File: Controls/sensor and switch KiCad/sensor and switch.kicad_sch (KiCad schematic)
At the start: 27 parts, among them U10 Encoder Breakout Board, U12 Spark MAX Motor Controller, U13 Max Breakout Board, U14 Encoder Breakout Board, U16 Spark MAX Motor Controller, U17 Max Breakout Board, U18 Encoder Breakout Board, U2 Jetson Nano, U20 Spark MAX Motor Controller, U21 Max Breakout Board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

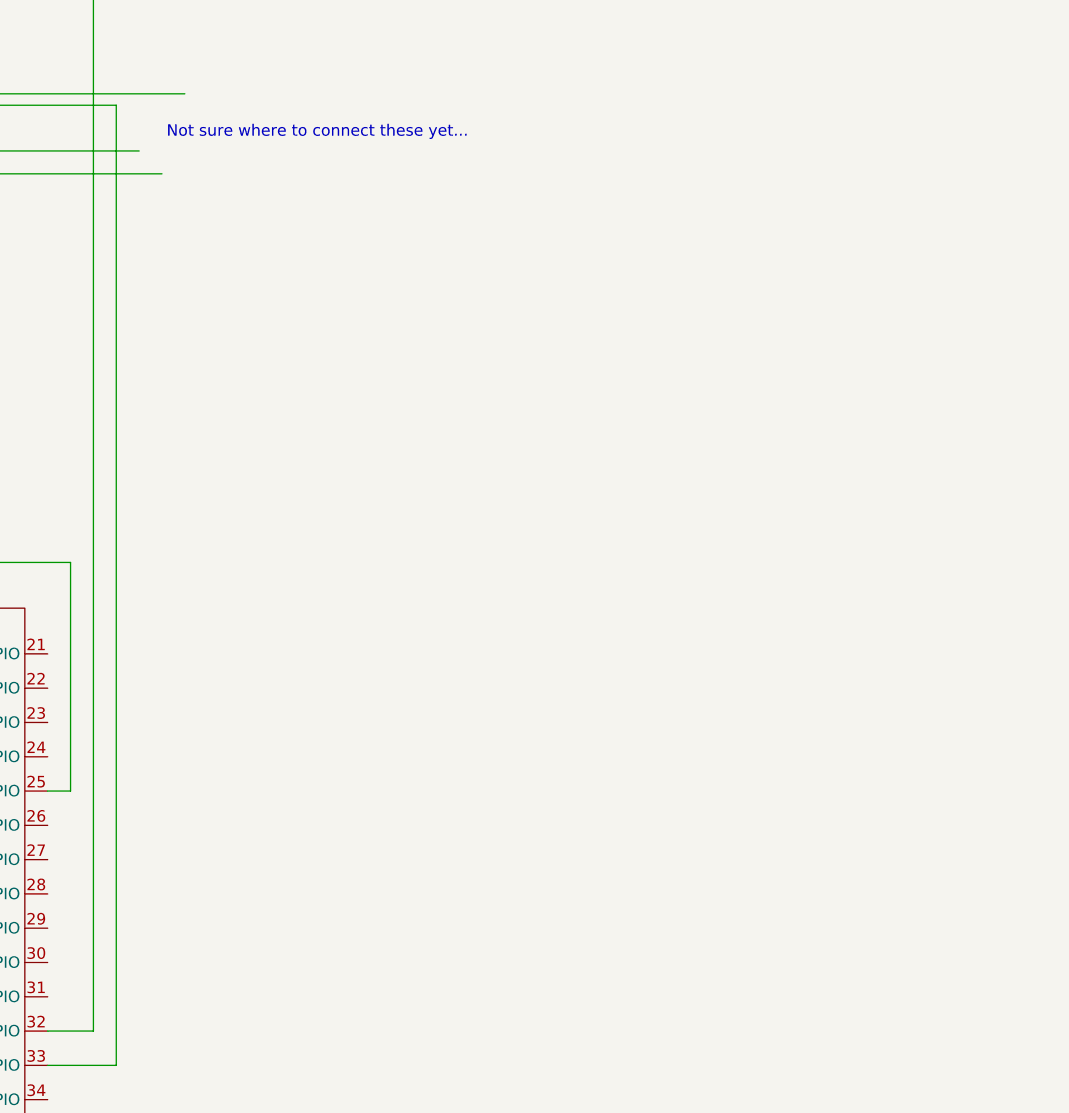
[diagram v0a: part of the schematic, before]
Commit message: Added linear actuator
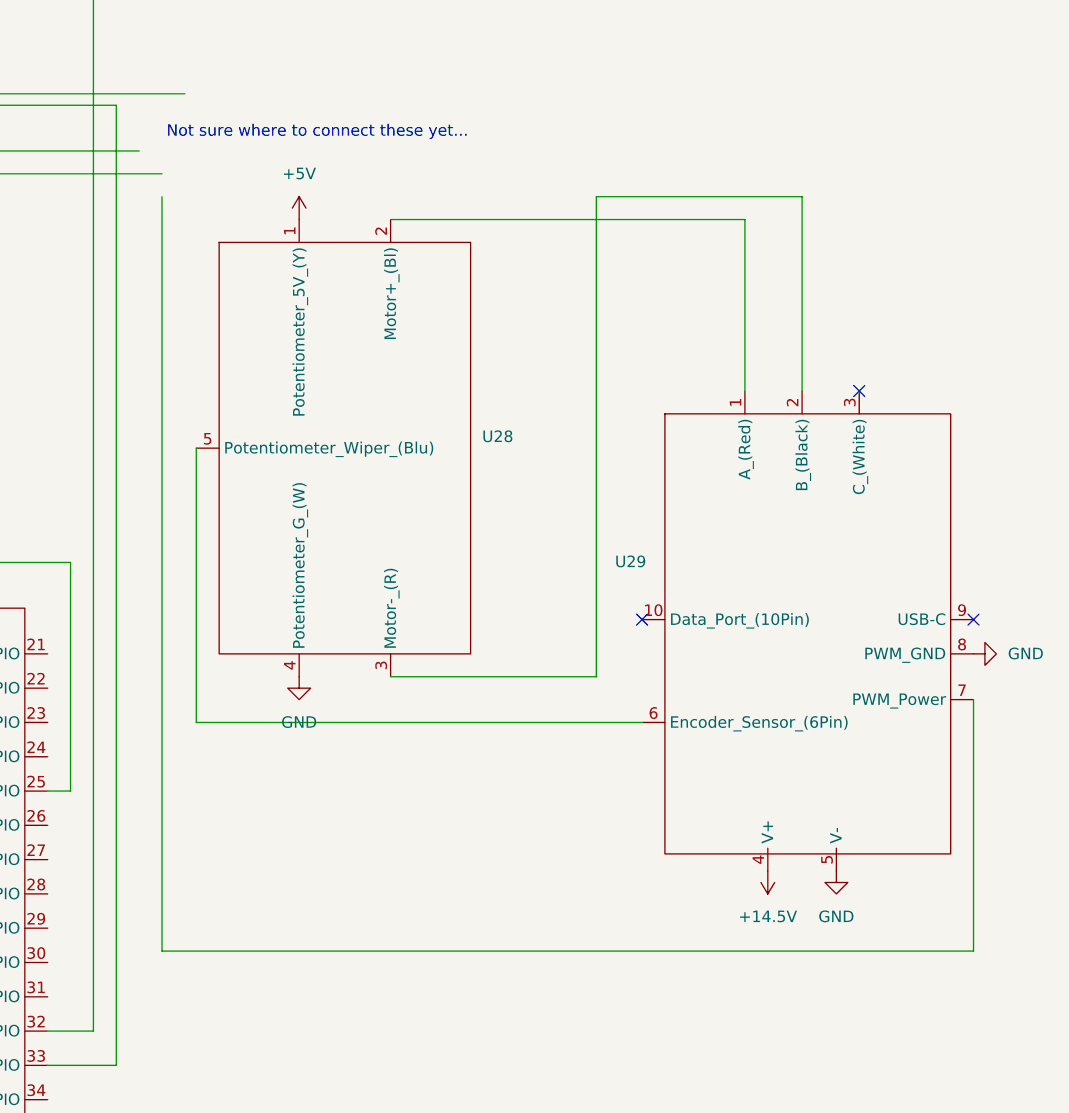
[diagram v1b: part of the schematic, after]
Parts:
- added U28: ~, symbol Lunabotics 2025-26:Feedback_Linear_Actuator
- added U29: ~, symbol Lunabotics 2025-26:Spark_MAX_Motor_Controller
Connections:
- net +5V: now also U28.1 (Potentiometer_5V_(Y))
- net GND: now also U28.4 (Potentiometer_G_(W)), U29.5 (V-), U29.8 (PWM_GND)
- new net: U28.2 (Motor+_(Bl)), U29.1 (A_(Red))
- new net: U28.3 (Motor-_(R)), U29.2 (B_(Black))
- new net: U28.5 (Potentiometer_Wiper_(Blu)), U29.6 (Encoder_Sensor_(6Pin))
- new net +14.5V: U29.4 (V+)
- no-connect marks 89 -> 92

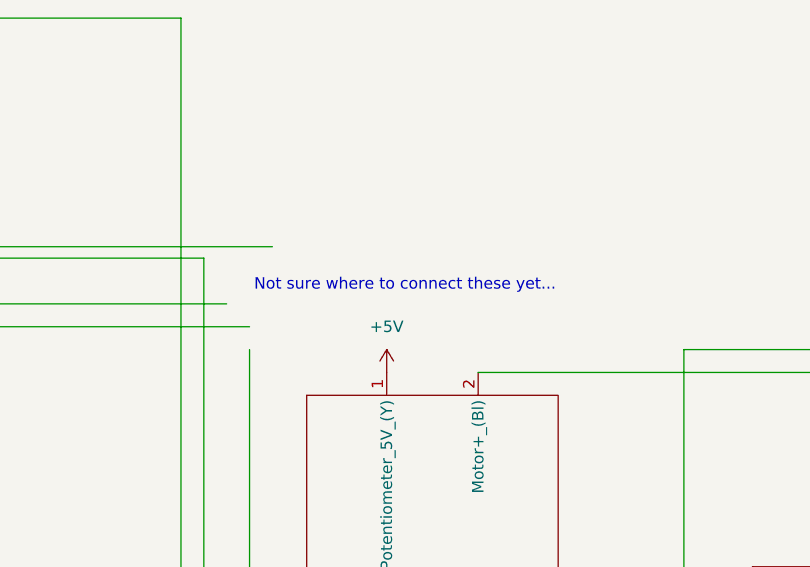
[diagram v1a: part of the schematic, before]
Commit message: Ported Linear Actuator to other schematics
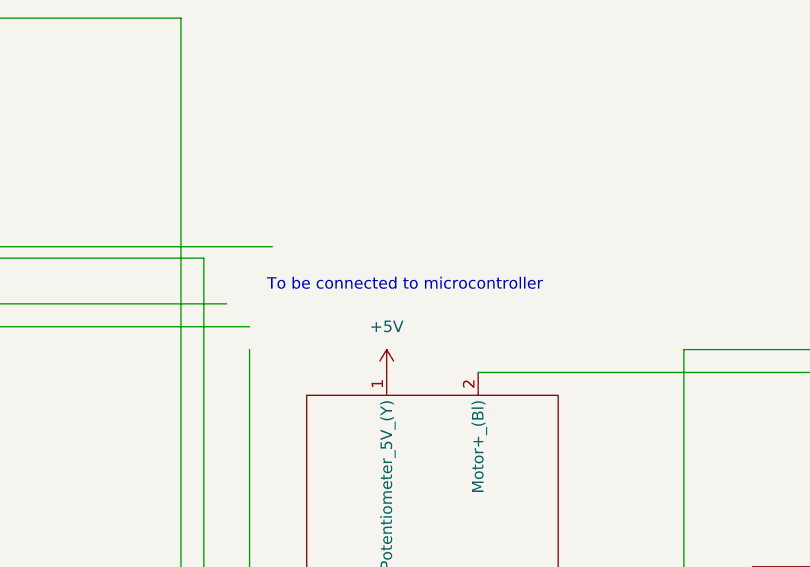
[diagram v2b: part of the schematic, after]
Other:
- note added: "To be connected to microcontroller"
- note removed: "Not sure where to connect these yet..."
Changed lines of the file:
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@@
 	(generator_version "9.0")
 	(paper "A2")
-	(text "Not sure where to connect these yet..."
+	(text "To be connected to microcontroller"
 		(exclude_from_sim no)
 		(at 488.442 165.608 0)

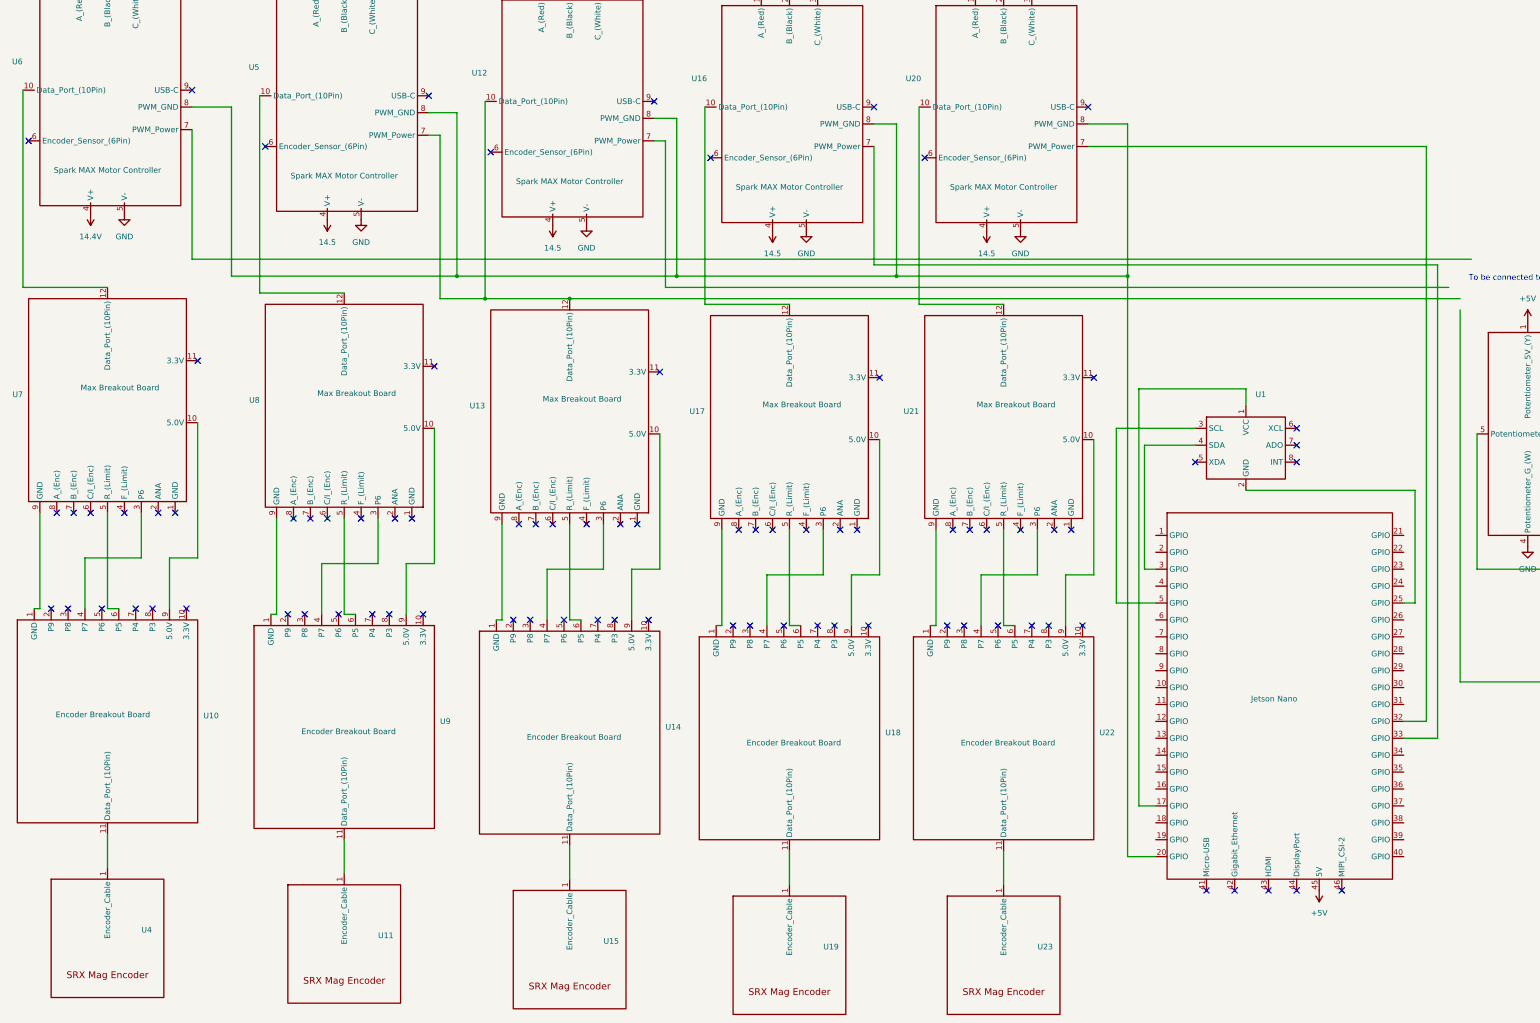
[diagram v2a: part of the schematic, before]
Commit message: Finalized Schematics with linear actuator and updated encoder
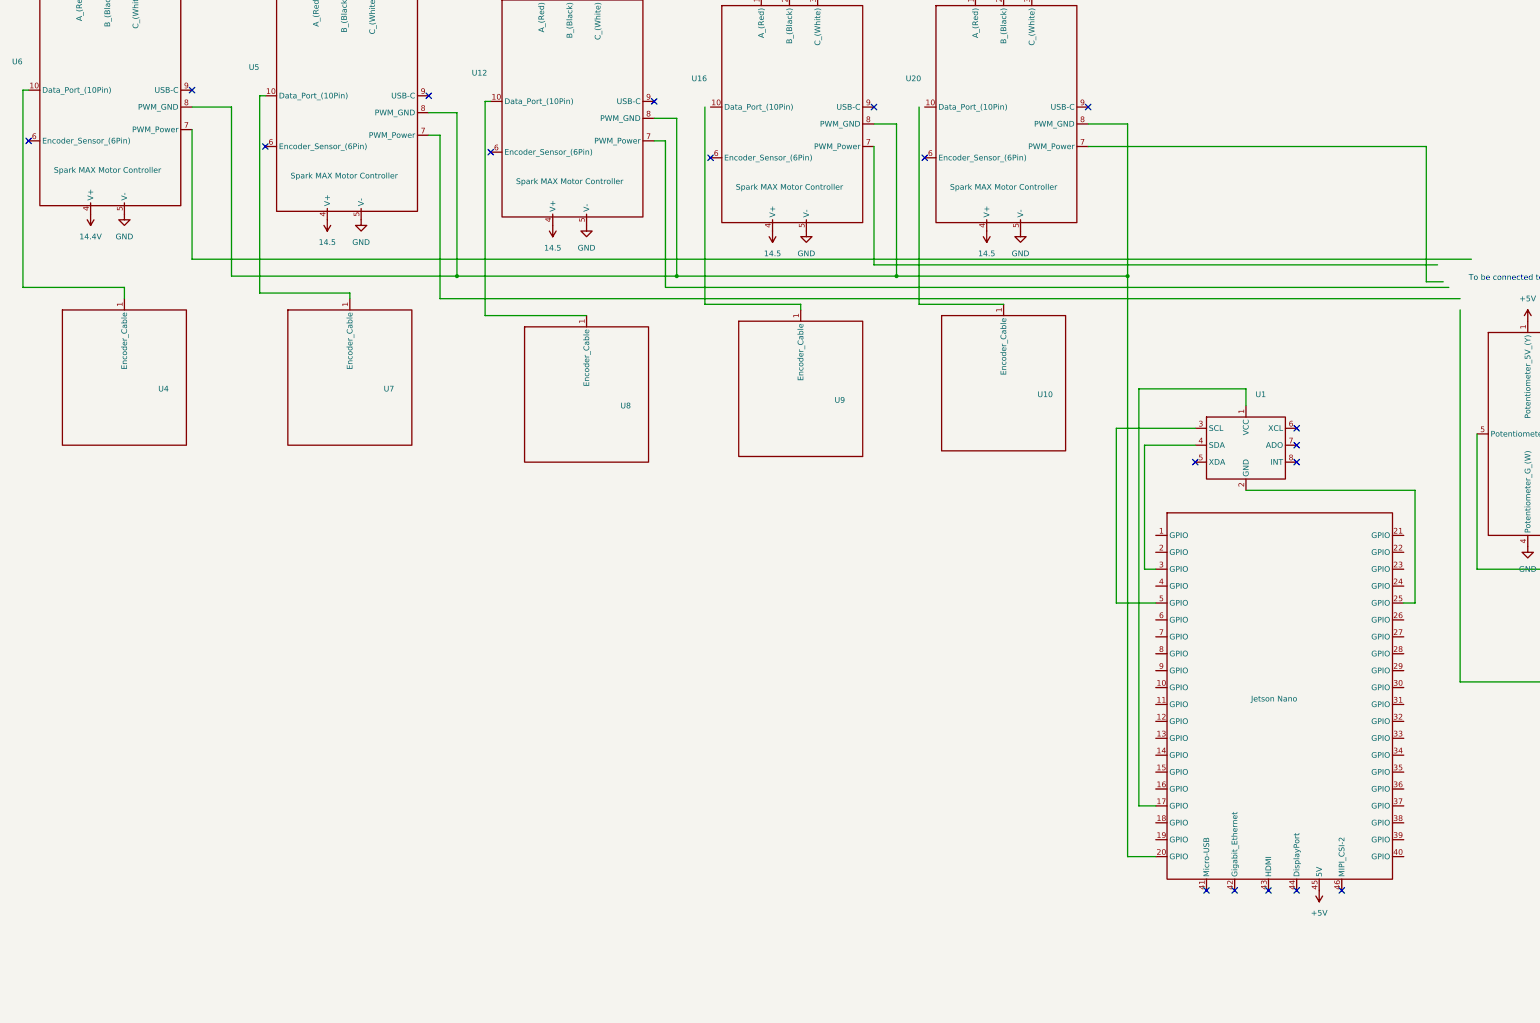
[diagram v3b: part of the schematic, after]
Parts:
- removed U10, U14, U18, U22, U9: Encoder Breakout Board, symbol Lunabotics 2025-26:Breakout_Board_Mag-Board
- removed U11, U15, U19, U23, U4: ~, symbol Lunabotics 2025-26:SRX_Mag_Encoder
- removed U13, U17, U21, U7, U8: Max Breakout Board, symbol Lunabotics 2025-26:Breakout_Board_Max-Board
- added U10, U4, U7, U8, U9: ~, symbol Lunabotics 2025-26:REV_Through_Bore_Encoder
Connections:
- net at U5.10 (Data_Port_(10Pin)): now also U7.1 (Encoder_Cable)
- net at U12.10 (Data_Port_(10Pin)): now also U8.1 (Encoder_Cable); no longer U5.7 (PWM_Power)
- net at U6.10 (Data_Port_(10Pin)): now also U4.1 (Encoder_Cable)
- net at U20.7 (PWM_Power): no longer U2.32 (GPIO)
- net at U2.33 (GPIO): no longer U16.7 (PWM_Power)
- no-connect marks 92 -> 27
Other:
- moved on the sheet: U12, U16, U20, U5, U6

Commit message: Updated Schematics & Library
Added Alternate Encoder to library and schematics, allows correct connection for Spark MAX to Neos. Also removed incorrect connection of linear actuator "encoder" to Spark MAX.
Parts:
- added U11, U13, U14, U15, U17: ~, symbol Lunabotics 2025-26:Rev_Alternate_Encoder_Adaptor
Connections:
- net at U10.1 (Encoder_Cable): now also U17.2 (Encoder_Plug)
- net at U12.10 (Data_Port_(10Pin)): now also U14.1 (Spark_MAX_Connection); no longer U8.1 (Encoder_Cable)
- net at U6.10 (Data_Port_(10Pin)): now also U11.1 (Spark_MAX_Connection); no longer U4.1 (Encoder_Cable)
- net at U28.5 (Potentiometer_Wiper_(Blu)): no longer U29.6 (Encoder_Sensor_(6Pin))
- net at U7.1 (Encoder_Cable): now also U13.2 (Encoder_Plug); no longer U5.10 (Data_Port_(10Pin))
- net at U9.1 (Encoder_Cable): now also U15.2 (Encoder_Plug)
- net at U20.10 (Data_Port_(10Pin)): now also U17.1 (Spark_MAX_Connection)
- new net: U11.2 (Encoder_Plug), U4.1 (Encoder_Cable)
- new net: U14.2 (Encoder_Plug), U8.1 (Encoder_Cable)
- new net: U13.1 (Spark_MAX_Connection), U5.10 (Data_Port_(10Pin))
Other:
- moved on the sheet: U10, U4, U7, U8, U9

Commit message: Updated controls and overall schematic
Not as many encoders are needed, so they were removed from the schematics.
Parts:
- removed U11, U13, U14, U15: ~, symbol Lunabotics 2025-26:Rev_Alternate_Encoder_Adaptor
- removed U4, U7, U8, U9: ~, symbol Lunabotics 2025-26:REV_Through_Bore_Encoder
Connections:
- no-connect marks 27 -> 31
